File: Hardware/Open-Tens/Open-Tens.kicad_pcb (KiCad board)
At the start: 2 copper layers, 53 parts, among them J1 Conn_01x02, J3 Conn_01x04_Female, Q1 IRF540N, Q2 IRF540N, Q3 Q_PMOS_DGS, SW1 SW_Push, SW2 SW_Push, U2 XC6206P332MR, U3 STM32F103C8T6, Y1 8MHz

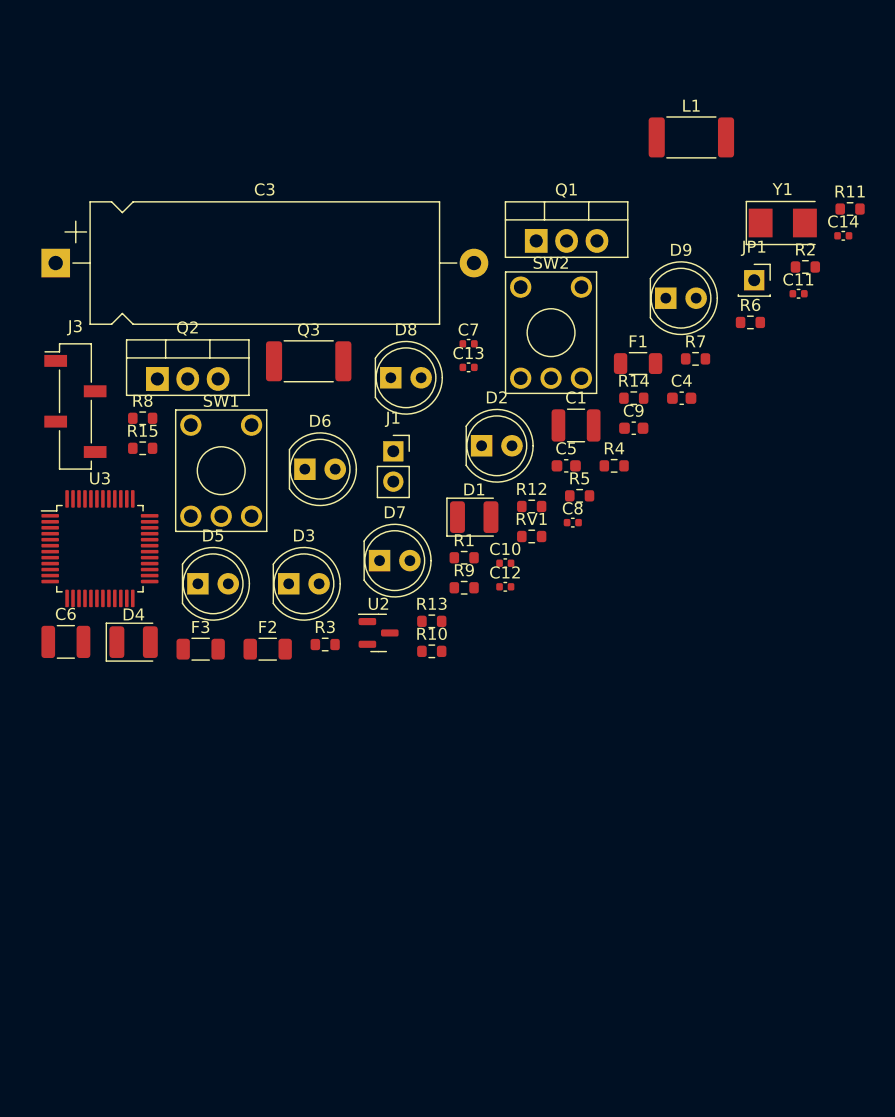
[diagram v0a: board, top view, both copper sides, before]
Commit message: Fiz um roteamento completo mas vou revisar e refazer
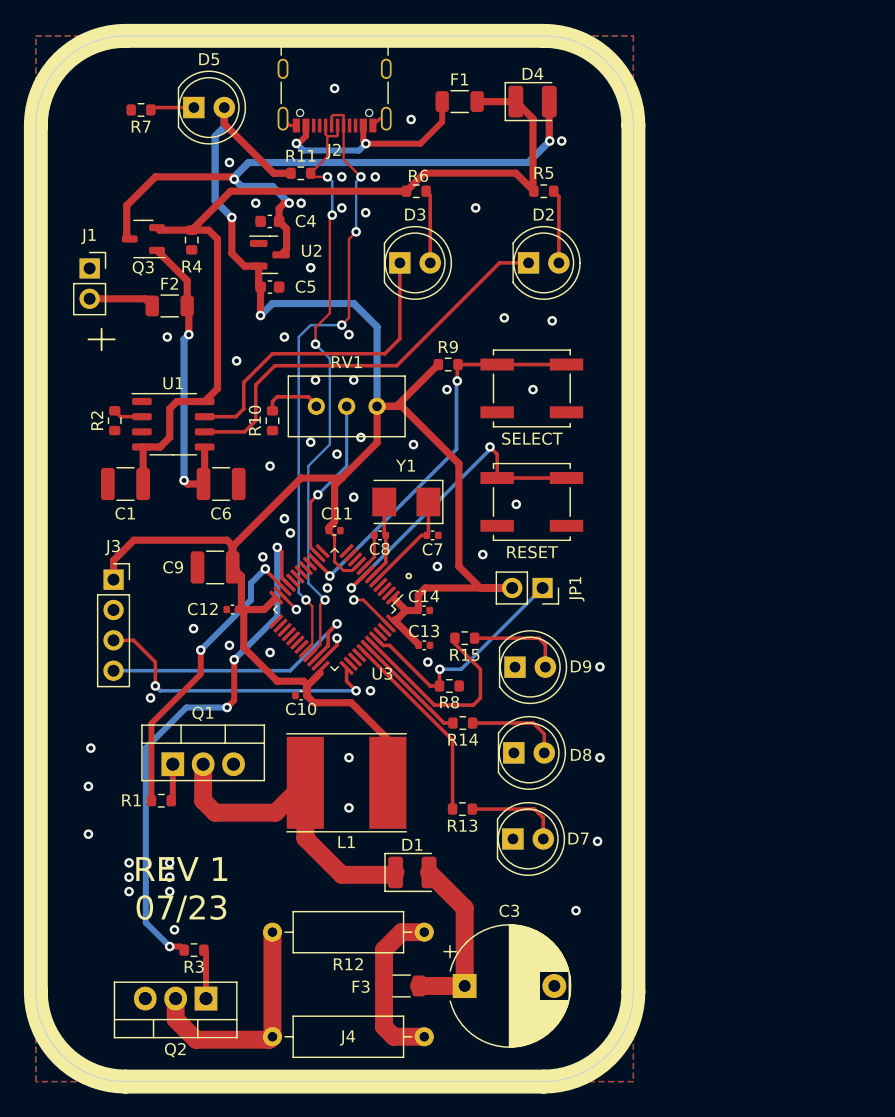
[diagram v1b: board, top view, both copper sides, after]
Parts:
- removed D6: BLUE, LED_THT:LED_D5.0mm_FlatTop
- removed SW1, SW2: SW_Push, Button_Switch_THT:KSA_Tactile_SPST
- added G***: LOGO, LOGO, B.Cu at (155.1, 104.2)
- added J2: CSP-USC16-TR, Connector_USB:USB_C_Receptacle_Palconn_UTC16-G, F.Cu at (154.8, 62.2)
- added J4: Conn_01x02, Resistor_THT:R_Axial_DIN0309_L9.0mm_D3.2mm_P12.70mm_Horizontal, F.Cu at (162.3, 140.9)
- added RESET: SW_Push, Button_Switch_SMD:SW_Push_1P1T_NO_CK_KSC6xxJ, F.Cu at (171.3, 96.2)
- added SELECT: SW_Push, Button_Switch_SMD:SW_Push_1P1T_NO_CK_KSC6xxJ, F.Cu at (171.3, 86.7)
- added U1: TP4056, Package_SO:SOP-8_3.9x4.9mm_P1.27mm, F.Cu at (141.3, 89.7)
- C3: footprint Capacitor_THT:CP_Axial_L29.0mm_D10.0mm_P35.00mm_Horizontal -> Capacitor_THT:CP_Radial_D10.0mm_P7.50mm
- C9: value 4u7 -> 10u; footprint Capacitor_SMD:C_0603_1608Metric -> Capacitor_SMD:C_1210_3225Metric
- J3: footprint Connector_PinSocket_2.54mm:PinSocket_1x04_P2.54mm_Vertical_SMD_Pin1Left -> Connector_PinSocket_2.54mm:PinSocket_1x04_P2.54mm_Vertical
- JP1: footprint Connector_PinSocket_2.54mm:PinSocket_1x01_P2.54mm_Vertical -> Connector_PinSocket_2.54mm:PinSocket_1x02_P2.54mm_Vertical
- L1: footprint Inductor_SMD:L_2512_6332Metric -> Inductor_SMD:L_Taiyo-Yuden_NR-80xx_HandSoldering
- Q3: footprint Inductor_SMD:L_2512_6332Metric -> Package_TO_SOT_SMD:SOT-23-3
- R12: value 1k5 -> 1M; footprint Resistor_SMD:R_0603_1608Metric -> Resistor_THT:R_Axial_DIN0309_L9.0mm_D3.2mm_P12.70mm_Horizontal
- RV1: footprint Resistor_SMD:R_0603_1608Metric -> Potentiometer_THT:Potentiometer_Bourns_3296W_Vertical
- moved C3 69.5 mm to (165.7, 136.7)
- moved L1 61.2 mm to (155.8, 119.7), turned to 180 degrees
- moved R2 59.2 mm to (136.4, 89.4), turned to 90 degrees
- moved D4 56.2 mm to (171.4, 62.7)
- moved Q1 53.3 mm to (141.3, 118.1)
- moved Q2 52.0 mm to (144.0, 137.8), turned to 180 degrees
- moved R7 50.9 mm to (138.6, 63.4), turned to 180 degrees
- moved C14 47.0 mm to (162.3, 105.3)
- moved R11 46.1 mm to (152.0, 68.7)
- moved C11 43.6 mm to (154.8, 98.6)
- moved R4 40.1 mm to (142.8, 74.3), turned to 90 degrees
- moved D5 39.9 mm to (143.0, 63.2)
- moved Y1 39.2 mm to (160.8, 96.2), turned to 180 degrees
- moved C1 38.0 mm to (137.3, 94.7), turned to 180 degrees
- moved C4 37.5 mm to (149.4, 72.7), turned to 180 degrees
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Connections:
- R12 pad 1: Net-(D6-Pad1) -> PIN+
- R12 pad 2: GND -> PIN-
- U3 pad 11: /LED_STAT -> unconnected-(U3-Pad11)
- U3 pad 21: PB10 -> FREQ_CTRL
- U3 pad 22: PB11 -> AMP_CTRL
- U3 pad 41: PB5 -> LED_ON
- U3 pad 42: PB6 -> LED_CONT
- U3 pad 43: PB7 -> LED_BURST
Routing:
- net +3.3V: track 0.00 -> 171.3 mm, vias 0 -> 2
- net VBUS: track 0.00 -> 73.5 mm
- net VCC: track 0.00 -> 54.9 mm, vias 0 -> 3
- net USB_D-: track 0.00 -> 51.6 mm, vias 0 -> 4
- net USB_D+: track 0.00 -> 51.0 mm, vias 0 -> 4
- net FREQ_CTRL: track 0.00 -> 45.7 mm, vias 0 -> 4
- net Net-(D2-Pad1): track 0.00 -> 34.7 mm
- net PIN_BOT: track 0.00 -> 33.1 mm, vias 0 -> 2
- net RESET: track 0.00 -> 27.2 mm, vias 0 -> 2
- net Net-(D3-Pad1): track 0.00 -> 26.7 mm
- net Net-(D1-Pad1): track 0.00 -> 26.6 mm
- net AMP_CTRL: track 0.00 -> 25.7 mm, vias 0 -> 2
- net SWCLK: track 0.00 -> 25.5 mm, vias 0 -> 2
- net +BATT: track 0.00 -> 25.4 mm, vias 0 -> 2
- net SWDIO: track 0.00 -> 24.1 mm, vias 0 -> 1
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- added copper zone on B.Cu, net GND
- added copper zone on F.Cu, net GND
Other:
- board outline added: 50 x 87.5 mm
- board text added: "REV 1 07/23"
